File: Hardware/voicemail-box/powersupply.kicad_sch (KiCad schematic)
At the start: 1 part, among them U4 R-78B3.3-2.0

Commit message: schematic draft
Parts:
- added J701: USB_C_Receptacle_PowerOnly_6P, Connector_USB:USB_C_Receptacle_HRO_TYPE-C-31-M-17, symbol Connector:USB_C_Receptacle_PowerOnly_6P
- added R701, R702: 5k1, PCM_4ms_Resistor:R_0603, symbol Device:R
- added U702: TC2015-1.8VxCTTR, Package_TO_SOT_SMD:SOT-23-5, symbol Regulator_Linear:TC2015-1.8VxCTTR
- renumbered U4 to U701
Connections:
- net +5V: now reaches U701.1 (IN)
- net +5V: now also J701.A9 (VBUS), J701.B9 (VBUS)
- net GND: now reaches U701.2 (GND)
- net GND: now also J701.A12 (GND), J701.B12 (GND), J701.S1 (SHIELD), R701.2, R702.2, U702.2 (GND)
- net +3.3V: now reaches U701.3 (OUT)
- net +3.3V: now also U702.1 (VIN), U702.3 (ON/~{OFF})
- new net: J701.B5 (CC2), R701.1
- new net: J701.A5 (CC1), R702.1
- new net +1V8: U702.4 (BP), U702.5 (VOUT)
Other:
- note added: "Caps + Beads needed"
- moved on the sheet: U701

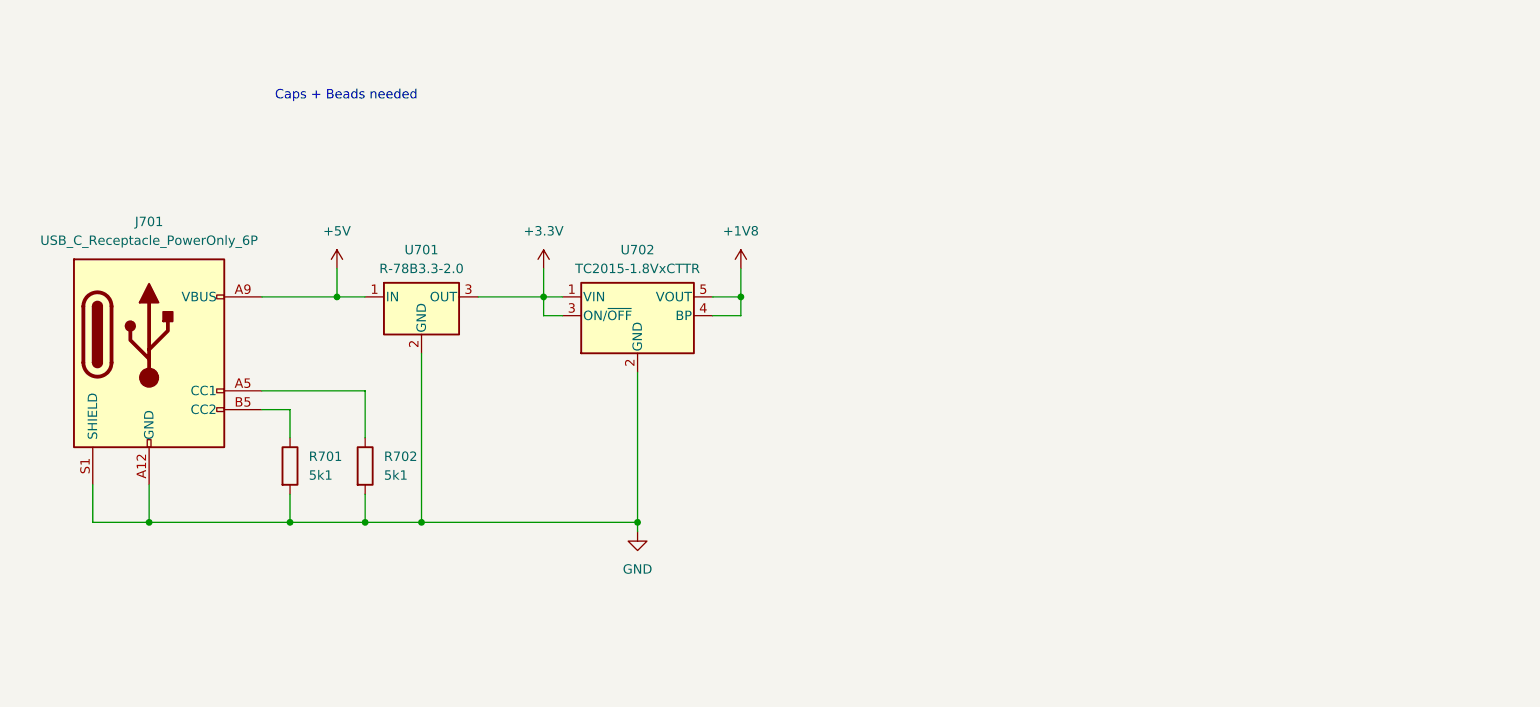
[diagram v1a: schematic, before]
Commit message: HW Layout progress todo: + Antenna + Audio Jacks + Planes (Supply only)
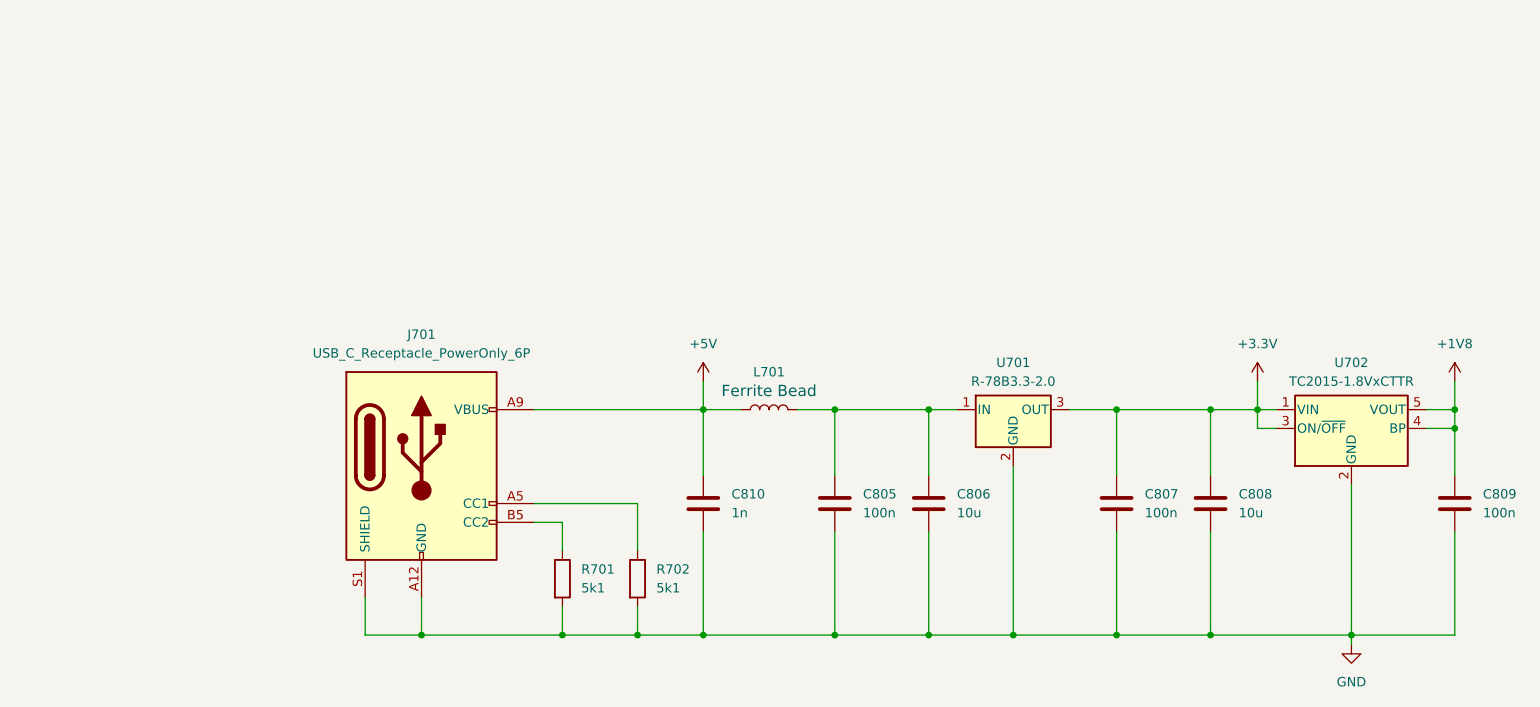
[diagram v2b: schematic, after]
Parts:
- added C805, C807, C809: 100n, Capacitor_SMD:C_0603_1608Metric_Pad1.08x0.95mm_HandSolder, symbol Device:C
- added C806, C808: 10u, Capacitor_SMD:C_0805_2012Metric_Pad1.18x1.45mm_HandSolder, symbol Device:C
- added C810: 1n, Capacitor_SMD:C_0603_1608Metric_Pad1.08x0.95mm_HandSolder, symbol Device:C
- added L701: FerriteBead_0603_1.5A, Inductor_SMD:L_0603_1608Metric_Pad1.05x0.95mm_HandSolder, symbol PCM_4ms_Inductor:FerriteBead_0603_1.5A
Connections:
- net +1V8: now also C809.1
- net +3.3V: now also C807.1, C808.1
- net +5V: now also C810.1, L701.1; no longer U701.1 (IN)
- net GND: now also C805.2, C806.2, C807.2, C808.2, C809.2, C810.2
- new net: C805.1, C806.1, L701.2, U701.1 (IN)
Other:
- note removed: "Caps + Beads needed"
- moved on the sheet: J701, R701, R702, U701, U702

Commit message: schema review
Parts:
- R701, R702: footprint PCM_4ms_Resistor:R_0603 -> Resistor_SMD:R_0603_1608Metric_Pad0.98x0.95mm_HandSolder
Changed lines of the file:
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@@
 			)
 		)
-		(property "Footprint" "PCM_4ms_Resistor:R_0603"
+		(property "Footprint" "Resistor_SMD:R_0603_1608Metric_Pad0.98x0.95mm_HandSolder"
 			(at 87.122 100.33 90)
 			(effects
@@
 			)
 		)
-		(property "Footprint" "PCM_4ms_Resistor:R_0603"
+		(property "Footprint" "Resistor_SMD:R_0603_1608Metric_Pad0.98x0.95mm_HandSolder"
 			(at 97.282 100.33 90)
 			(effects

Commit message: ~layout
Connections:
- net +1V8: no longer U702.4 (BP)
- net +3.3V renamed +3V3
- no-connect marks 0 -> 1
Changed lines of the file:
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@@
-	)
-	(junction
-		(at 209.55 80.01)
-		(diameter 0)
-		(color 0 0 0 0)
 	)
 	(junction
@@
 		(color 0 0 0 0)
 	)
+	(no_connect
+		(at 205.74 80.01)
+	)
 	(wire
 		(pts
@@
 	(wire
 		(pts
-			(xy 205.74 80.01) (xy 209.55 80.01)
-		)
-		(stroke
-			(width 0)
-			(type default)
-		)
-	)
-	(wire
-		(pts
 			(xy 99.06 107.95) (xy 107.95 107.95)
 		)
@@
 	(wire
 		(pts
-			(xy 209.55 80.01) (xy 209.55 77.47)
-		)
-		(stroke
-			(width 0)
-			(type default)
-		)
-	)
-	(wire
-		(pts
 			(xy 209.55 73.66) (xy 209.55 77.47)
 		)
@@
 	(wire
 		(pts
-			(xy 209.55 80.01) (xy 209.55 86.36)
+			(xy 209.55 77.47) (xy 209.55 86.36)
 		)
 		(stroke
@@
 	)
 	(symbol
+		(lib_name "+3V3_1")
+		(lib_id "power:+3V3")
+		(at 182.88 73.66 0)
+		(mirror y)
+		(unit 1)
+		(exclude_from_sim no)
+		(in_bom yes)
+		(on_board yes)
+		(dnp no)
+		(fields_autoplaced yes)
+		(property "Reference" "#PWR0409"
+			(at 182.88 77.47 0)
+			(effects
+				(font
+					(size 1.27 1.27)
+				)
+				(hide yes)
+			)
+		)
+		(property "Value" "+3V3"
+			(at 182.88 68.58 0)
+			(effects
+				(font
+					(size 1.27 1.27)
+				)
+			)
+		)
+		(property "Footprint" ""
+			(at 182.88 73.66 0)
+			(effects
+				(font
+					(size 1.27 1.27)
+				)
+				(hide yes)
+			)
+		)
+		(property "Datasheet" ""
+			(at 182.88 73.66 0)
+			(effects
+				(font
+					(size 1.27 1.27)
+				)
+				(hide yes)
+			)
+		)
+		(property "Description" "Power symbol creates a global label with name \"+3V3\""
+			(at 182.88 73.66 0)
+			(effects
+				(font
+					(size 1.27 1.27)
+				)
+				(hide yes)
+			)
+		)
+		(pin "1"
+		)
+		(instances
+			(project "voicemail-box"
+				(path "/e63e39d7-6ac0-4ffd-8aa3-1841a4541b55/f6dd423f-bceb-4b7e-85cb-bb54e6f6d80b"
+					(reference "#PWR0409")
+					(unit 1)
+				)
+			)
+		)
+	)
+	(symbol
 		(lib_id "Device:C")
 		(at 176.53 90.17 0)
@@
 					(unit 1)
 				)
-			)
-		)
-	)
-	(symbol
-		(lib_id "power:+3.3V")
-		(at 182.88 73.66 0)
-		(unit 1)
-		(exclude_from_sim no)
-		(in_bom yes)
-		(on_board yes)
-		(dnp no)
-		(fields_autoplaced yes)
-		(property "Reference" "#PWR0702"
-			(at 182.88 77.47 0)
-			(effects
-				(font
-					(size 1.27 1.27)
-				)
-				(hide yes)
-			)
-		)
-		(property "Value" "+3.3V"
-			(at 182.88 68.58 0)
-			(effects
-				(font
-					(size 1.27 1.27)
-				)
-			)
-		)
-		(property "Footprint" ""
-			(at 182.88 73.66 0)
-			(effects
-				(font
-					(size 1.27 1.27)
-				)
-				(hide yes)
-			)
-		)
-		(property "Datasheet" ""
-			(at 182.88 73.66 0)
-			(effects
-				(font
-					(size 1.27 1.27)
-				)
-				(hide yes)
-			)
-		)
-		(property "Description" "Power symbol creates a global label with name \"+3.3V\""
-			(at 182.88 73.66 0)
-			(effects
-				(font
-					(size 1.27 1.27)
-				)
-				(hide yes)
-			)
-		)
-		(pin "1"
-		)
-		(instances
-			(project "voicemail-box"
-				(path "/e63e39d7-6ac0-4ffd-8aa3-1841a4541b55/f6dd423f-bceb-4b7e-85cb-bb54e6f6d80b"
-					(reference "#PWR0702")
-					(unit 1)
-				)
